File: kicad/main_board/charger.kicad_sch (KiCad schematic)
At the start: 72 parts, among them J4 BAT, J5 BAT_LINK, Q3 CSD17551Q3A, Q4 CSD17551Q3A, Q5 CSD17551Q3A, Q6 CSD17551Q3A, Q7 CSD25402Q3A, U4 BQ25703A

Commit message: add I2S link
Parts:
- added TP7: ~{BAT_INT}, TestPoint:TestPoint_Pad_D1.0mm, symbol Connector:TestPoint_Small
- renumbered TP9 to TP10, TP10 to TP11, TP11 to TP12, TP12 to TP13, TP7 to TP8, TP8 to TP9
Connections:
- net ~{BAT_INT}: no longer names the net of D2.2 (A), R22.1
- net ~{BAT_INT}: now also TP7.1
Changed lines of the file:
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@@
 	(title_block
 		(title "SW32 - Main Board")
-		(date "2024-05-22")
+		(date "2024-05-23")
 		(rev "1")
 		(company "saawsm")
@@
 	)
 	(junction
-		(at 59.69 186.69)
-		(diameter 0)
-		(color 0 0 0 0)
-	)
-	(junction
 		(at 143.51 55.88)
 		(diameter 0)
@@
 	)
 	(junction
+		(at 59.69 186.69)
+		(diameter 0)
+		(color 0 0 0 0)
+	)
+	(junction
 		(at 256.54 114.3)
 		(diameter 0)
@@
 	(wire
 		(pts
+			(xy 59.69 186.69) (xy 67.31 186.69)
+		)
+		(stroke
+			(width 0)
+			(type default)
+		)
+	)
+	(wire
+		(pts
 			(xy 106.68 134.62) (xy 115.57 134.62)
 		)
@@
 	(wire
 		(pts
-			(xy 59.69 186.69) (xy 67.31 186.69)
-		)
-		(stroke
-			(width 0)
-			(type default)
-		)
-	)
-	(wire
-		(pts
 			(xy 240.03 62.23) (xy 241.3 62.23)
 		)
@@
 		)
 	)
-	(hierarchical_label "~{BAT_INT}"
-		(shape output)
-		(at 67.31 186.69 0)
-		(fields_autoplaced yes)
-		(effects
-			(font
-				(size 1.27 1.27)
-			)
-			(justify left)
-		)
-	)
 	(hierarchical_label "SDA"
 		(shape bidirectional)
@@
 		(on_board yes)
 		(dnp no)
-		(property "Reference" "TP8"
+		(property "Reference" "TP9"
 			(at 113.03 136.906 0)
 			(effects
@@
 			(project "main_board"
 				(path "/8e1f1504-76c2-49e6-9261-3c1190503f8c/1076a657-0b13-48f5-b500-e72d30eb3a1f"
-					(reference "TP8")
+					(reference "TP9")
 					(unit 1)
 				)
@@
 		(dnp no)
 		(fields_autoplaced yes)
-		(property "Reference" "TP7"
+		(property "Reference" "TP8"
 			(at 104.14 125.7299 0)
 			(effects
@@
 			(project "main_board"
 				(path "/8e1f1504-76c2-49e6-9261-3c1190503f8c/1076a657-0b13-48f5-b500-e72d30eb3a1f"
-					(reference "TP7")
+					(reference "TP8")
 					(unit 1)
 				)
@@
 		(dnp no)
 		(fields_autoplaced yes)
-		(property "Reference" "TP11"
+		(property "Reference" "TP12"
 			(at 267.97 151.13 0)
 			(effects
@@
 			(project "main_board"
 				(path "/8e1f1504-76c2-49e6-9261-3c1190503f8c/1076a657-0b13-48f5-b500-e72d30eb3a1f"
-					(reference "TP11")
+					(reference "TP12")
 					(unit 1)
 				)
@@
 		(dnp no)
 		(fields_autoplaced yes)
-		(property "Reference" "TP9"
+		(property "Reference" "TP10"
 			(at 203.2 21.5899 0)
 			(effects
@@
 			(project "main_board"
 				(path "/8e1f1504-76c2-49e6-9261-3c1190503f8c/1076a657-0b13-48f5-b500-e72d30eb3a1f"
-					(reference "TP9")
+					(reference "TP10")
 					(unit 1)
 				)
@@
 		(dnp no)
 		(fields_autoplaced yes)
-		(property "Reference" "TP10"
+		(property "Reference" "TP11"
 			(at 217.17 116.84 90)
 			(effects
@@
 			(project "main_board"
 				(path "/8e1f1504-76c2-49e6-9261-3c1190503f8c/1076a657-0b13-48f5-b500-e72d30eb3a1f"
-					(reference "TP10")
+					(reference "TP11")
+					(unit 1)
+				)
+			)
+		)
+	)
+	(symbol
+		(lib_id "Connector:TestPoint_Small")
+		(at 67.31 186.69 0)
+		(mirror y)
+		(unit 1)
+		(exclude_from_sim no)
+		(in_bom no)
+		(on_board yes)
+		(dnp no)
+		(fields_autoplaced yes)
+		(property "Reference" "TP7"
+			(at 68.58 185.4199 0)
+			(effects
+				(font
+					(size 1.27 1.27)
+				)
+				(justify right)
+			)
+		)
+		(property "Value" "~{BAT_INT}"
+			(at 68.58 187.9599 0)
+			(effects
+				(font
+					(size 1.27 1.27)
+				)
+				(justify right)
+			)
+		)
+		(property "Footprint" "TestPoint:TestPoint_Pad_D1.0mm"
+			(at 62.23 186.69 0)
+			(effects
+				(font
+					(size 1.27 1.27)
+				)
+				(hide yes)
+			)
+		)
+		(property "Datasheet" "~"
+			(at 62.23 186.69 0)
+			(effects
+				(font
+					(size 1.27 1.27)
+				)
+				(hide yes)
+			)
+		)
+		(property "Description" "test point"
+			(at 67.31 186.69 0)
+			(effects
+				(font
+					(size 1.27 1.27)
+				)
+				(hide yes)
+			)
+		)
+		(property "MPN" ""
+			(at 67.31 186.69 0)
+			(effects
+				(font
+					(size 1.27 1.27)
+				)
+				(hide yes)
+			)
+		)
+		(property "MPN_ALT" ""
+			(at 67.31 186.69 0)
+			(effects
+				(font
+					(size 1.27 1.27)
+				)
+				(hide yes)
+			)
+		)
+		(property "LCSC" ""
+			(at 67.31 186.69 0)
+			(effects
+				(font
+					(size 1.27 1.27)
+				)
+				(hide yes)
+			)
+		)
+		(property "MOUSER" ""
+			(at 67.31 186.69 0)
+			(effects
+				(font
+					(size 1.27 1.27)
+				)
+				(hide yes)
+			)
+		)
+		(pin "1"
+		)
+		(instances
+			(project "main_board"
+				(path "/8e1f1504-76c2-49e6-9261-3c1190503f8c/1076a657-0b13-48f5-b500-e72d30eb3a1f"
+					(reference "TP7")
 					(unit 1)
 				)
@@
 		(dnp no)
 		(fields_autoplaced yes)
-		(property "Reference" "TP12"
+		(property "Reference" "TP13"
 			(at 275.59 151.13 0)
 			(effects
@@
 			(project "main_board"
 				(path "/8e1f1504-76c2-49e6-9261-3c1190503f8c/1076a657-0b13-48f5-b500-e72d30eb3a1f"
-					(reference "TP12")
+					(reference "TP13")
 					(unit 1)
 				)

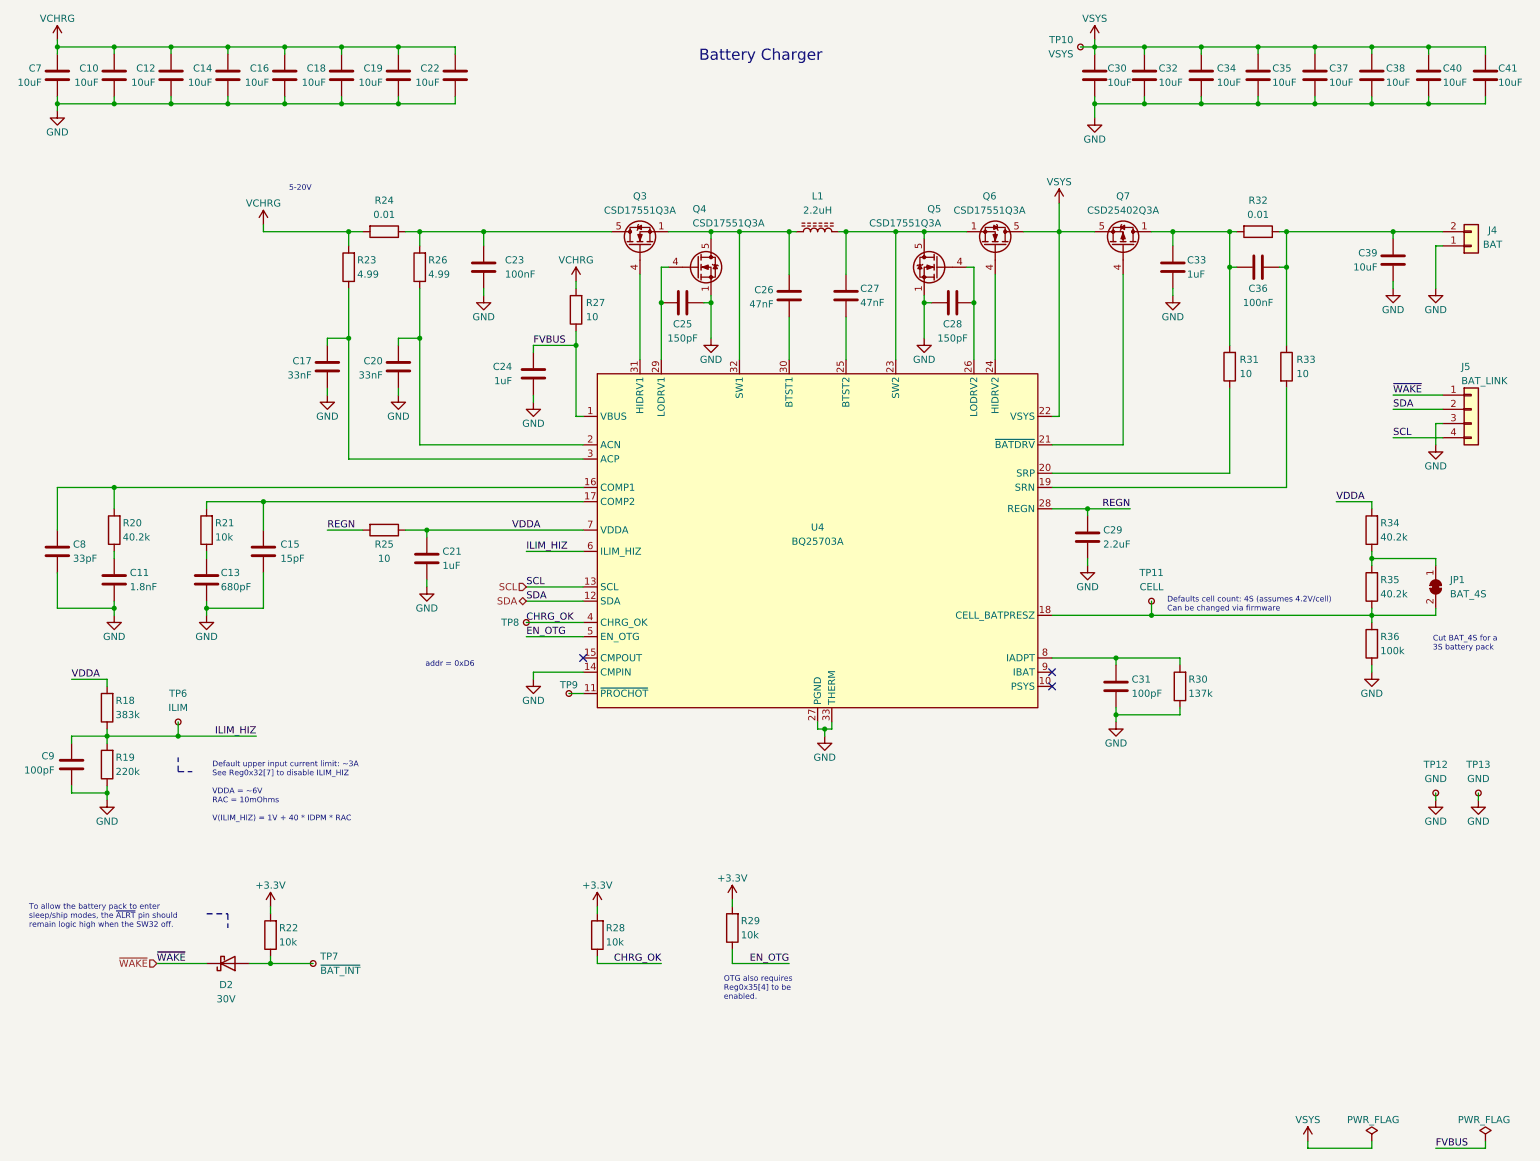
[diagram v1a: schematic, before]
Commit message: remove BAT_INT
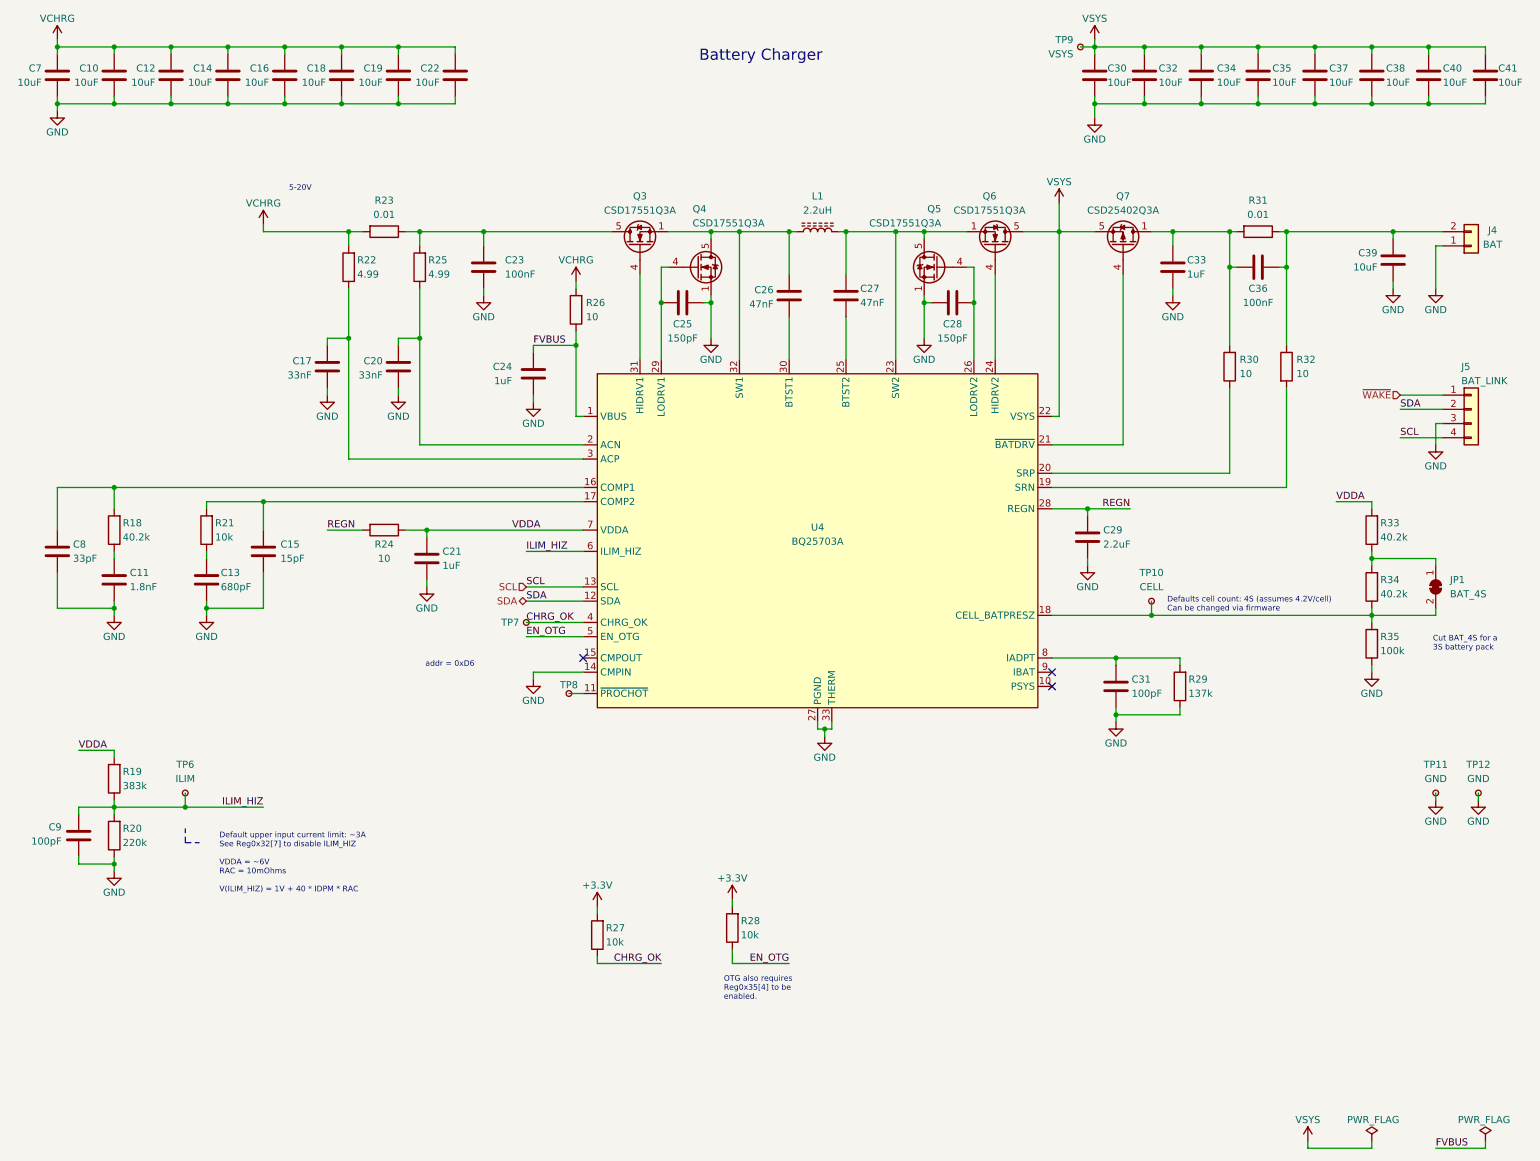
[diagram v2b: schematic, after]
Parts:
- removed D2: 30V, Diode_SMD:D_SOD-523, symbol Device:D_Schottky
- removed R22: 10k, Resistor_SMD:R_0603_1608Metric, symbol Device:R
- removed TP7: ~{BAT_INT}, TestPoint:TestPoint_Pad_D1.0mm, symbol Connector:TestPoint_Small
- renumbered R20 to R18, R18 to R19, R19 to R20, R23 to R22, R24 to R23, R25 to R24, R26 to R25, R27 to R26, R28 to R27, R29 to R28, R30 to R29, R31 to R30, R32 to R31, R33 to R32, R34 to R33, R35 to R34, R36 to R35, TP11 to TP10, TP12 to TP11, TP13 to TP12, TP8 to TP7, TP9 to TP8, TP10 to TP9
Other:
- note removed: "To allow the battery pack to enter sleep/ship modes, the ~{ALRT} pin should remain logic high when the SW32 off."
- moved on the sheet: C9, R19, R20, TP6

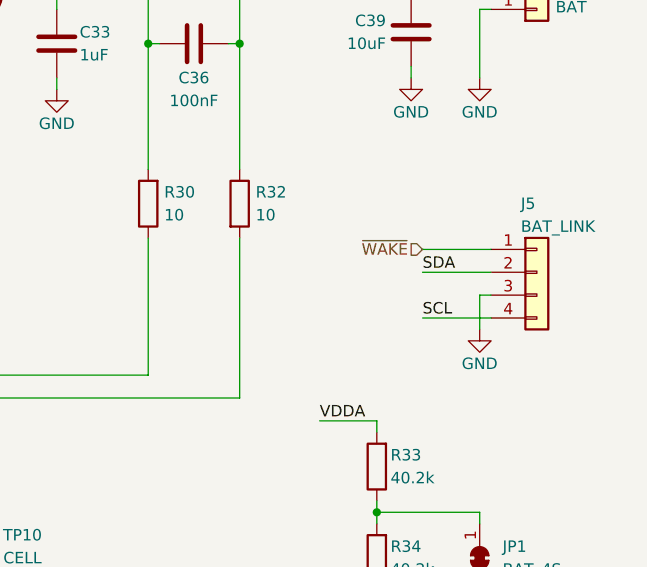
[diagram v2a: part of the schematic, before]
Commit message: fix BAT_LINK pinout for consistency
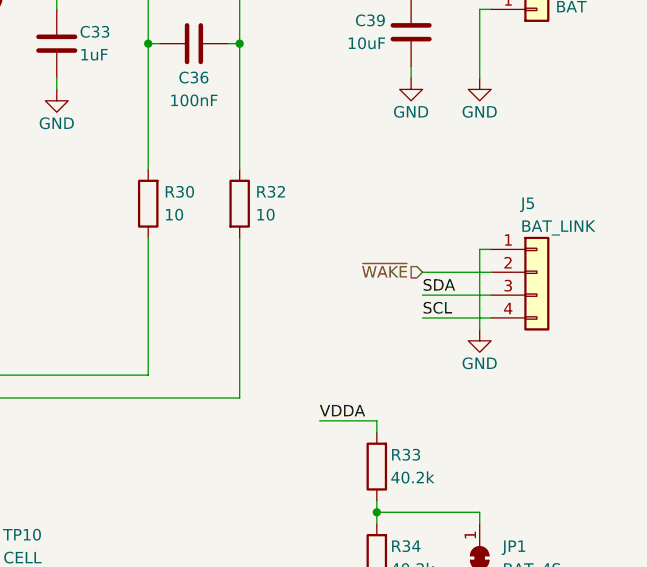
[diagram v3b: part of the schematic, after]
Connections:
- net GND: now also J5.1 (Pin_1); no longer J5.3 (Pin_3)
- net SDA: now also J5.3 (Pin_3); no longer J5.2 (Pin_2)
- net ~{WAKE}: now also J5.2 (Pin_2); no longer J5.1 (Pin_1)
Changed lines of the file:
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@@
 	(wire
 		(pts
-			(xy 267.97 90.17) (xy 269.24 90.17)
+			(xy 267.97 85.09) (xy 269.24 85.09)
 		)
 		(stroke
@@
 	(wire
 		(pts
-			(xy 267.97 93.98) (xy 267.97 90.17)
+			(xy 267.97 93.98) (xy 267.97 85.09)
 		)
 		(stroke
@@
 	(wire
 		(pts
-			(xy 261.62 85.09) (xy 269.24 85.09)
+			(xy 261.62 87.63) (xy 269.24 87.63)
 		)
 		(stroke
@@
 	(wire
 		(pts
-			(xy 261.62 87.63) (xy 269.24 87.63)
+			(xy 261.62 90.17) (xy 269.24 90.17)
 		)
 		(stroke
@@
 	)
 	(label "SDA"
-		(at 261.62 87.63 0)
+		(at 261.62 90.17 0)
 		(fields_autoplaced yes)
 		(effects
@@
 	(hierarchical_label "~{WAKE}"
 		(shape input)
-		(at 261.62 85.09 180)
+		(at 261.62 87.63 180)
 		(fields_autoplaced yes)
 		(effects

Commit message: update BOM prioritizing basic parts
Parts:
- added R84: 82k, Resistor_SMD:R_0603_1608Metric, symbol Device:R
- added R85: 1.2k, Resistor_SMD:R_0603_1608Metric, symbol Device:R
- added R86: 100k, Resistor_SMD:R_0603_1608Metric, symbol Device:R
- added R87: 10k, Resistor_SMD:R_0603_1608Metric, symbol Device:R
- C10, C12, C14, C16, C18, C19, C22, C30, C32, C34, C35, C37, C38, C39, C40, C41, C7: JLC (none) -> C440198; LCSC C2932476 -> (none); MOUSER 187-CL21A106KBYQNNE -> (none); MPN CL21A106KBYQNNE -> (none)
- C11: JLC (none) -> C318642; LCSC C318642 -> (none); MOUSER 187-CL10C182JB8NNNC -> (none); MPN CL10C182JB8NNNC -> (none)
- C13: JLC (none) -> C30816; LCSC C30816 -> (none); MOUSER 187-CL10C681JB8NNNC -> (none); MPN CL10C681JB8NNNC -> (none)
- C15: JLC (none) -> C1644; LCSC C1644 -> (none); MOUSER 187-CL10C150JB8NNNC -> (none); MPN CL10C150JB8NNNC -> (none)
- C17, C20: JLC (none) -> C21117; LCSC C21117 -> (none); MOUSER 187-CL10B333KB8NNNC -> (none); MPN CL10B333KB8NNNC -> (none)
- C21, C24, C33: JLC (none) -> C15849; LCSC C5199872 -> (none); MOUSER 187-CL10B105KB8NQNC -> (none); MPN CL10B105KB8NQNC -> (none)
- C23, C36: JLC (none) -> C14663; LCSC C1591 -> (none); MOUSER 187-CL10B104KB8NNNC -> (none); MPN CL10B104KB8NNNC -> (none)
- C25, C28: JLC (none) -> C37298; LCSC C37298 -> (none); MOUSER 187-CL10C151JB8NNNC -> (none); MPN CL10C151JB8NNNC -> (none)
- C26, C27: JLC (none) -> C1622; LCSC C1622 -> (none); MOUSER 187-CL10B473KB8NNNC -> (none); MPN CL10B473KB8NNNC -> (none)
- C29: JLC (none) -> C23630; LCSC C307463 -> (none); MOUSER 187-CL10A225KL8NNNC -> (none); MPN CL10A225KL8NNNC -> (none)
- C31, C9: JLC (none) -> C14858; LCSC C14858 -> (none); MOUSER 187-CL10C101JB8NNNC -> (none); MPN CL10C101JB8NNNC -> (none)
- C8: JLC (none) -> C1663; LCSC C1663 -> (none); MOUSER 187-CL10C330JB8NNNC -> (none); MPN CL10C330JB8NNNC -> (none)
- J4: footprint Connector_AMASS:AMASS_XT30UPB-F_1x02_P5.0mm_Vertical -> Connector_AMASS:AMASS_XT30UPB-M_1x02_P5.0mm_Vertical
- J5: footprint Connector_JST:JST_PH_B4B-PH-K_1x04_P2.00mm_Vertical -> Connector_JST:JST_XH_B4B-XH-A_1x04_P2.50mm_Vertical; LCSC (none) -> C7429634
- L1: JLC (none) -> C540967; LCSC C540967 -> (none); MOUSER 70-IHLP2525CZER2R2M1 -> (none); MPN IHLP2525CZER2R2M01 -> (none)
- Q3, Q4, Q5, Q6: JLC (none) -> C2876535; LCSC C2876535 -> (none); MOUSER 595-CSD17551Q3A -> (none); MPN CSD17551Q3A -> (none)
- Q7: JLC (none) -> C111356; LCSC C111356 -> (none); MOUSER 595-CSD25402Q3A -> (none); MPN CSD25402Q3A -> (none)
- R18, R33, R34: value 40.2k -> 39k; JLC (none) -> C23153; LCSC C137723 -> (none); MOUSER 603-RC0603FR-0740K2L -> (none); MPN RC0603FR-0740K2L -> (none)
- R19: value 383k -> 300k; JLC (none) -> C23024; LCSC C25816 -> (none); MOUSER 603-RC0603FR-07383KL -> (none); MPN RC0603FR-07383KL -> (none)
- R20: JLC (none) -> C22961; LCSC C22961 -> (none); MOUSER 603-RC0603FR-07220KL -> (none); MPN RC0603FR-07220KL -> (none)
- R21, R27, R28: JLC (none) -> C25804; LCSC C25804 -> (none); MOUSER 603-RC0603FR-0710KL -> (none); MPN RC0603FR-0710KL -> (none)
- R22, R25: JLC (none) -> C137704; LCSC C137704 -> (none); MOUSER 603-RC0603FR-074R99L -> (none); MPN RC0603FR-074R99L -> (none)
- R23, R31: JLC (none) -> C844910; LCSC C844910 -> (none); MOUSER 71-WSLP1206R0100FEA -> (none); MPN WSLP1206R0100FEA -> (none)
- R24, R26, R30, R32: JLC (none) -> C22859; LCSC C109318 -> (none); MOUSER 603-RC0603FR-0710RL -> (none); MPN RC0603FR-0710RL -> (none)
- R29: value 137k -> 27k; JLC (none) -> C22967; LCSC C22872 -> (none); MOUSER 603-RC0603FR-07137KL -> (none); MPN RC0603FR-07137KL -> (none)
- R35: JLC (none) -> C25803; LCSC C25803 -> (none); MOUSER 603-RC0603FR-07100KL -> (none); MPN RC0603FR-07100KL -> (none)
- U4: JLC (none) -> C188229; LCSC C188229 -> (none); MOUSER 595-BQ25703ARSNR -> (none); MPN BQ25703ARSNR -> (none)
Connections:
- net GND: now also R86.1; no longer R29.1
- net VDDA: now also R84.1; no longer R19.2
- net at C8.1, U4.16 (COMP1): now also R85.2; no longer R18.2
- new net: R18.2, R85.1
- new net: R19.2, R84.2
- new net: R86.2, R87.1
- new net: R29.1, R87.2
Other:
- note added: "137k changed to 100k+10k+27k to avoid basic part fee"
- note added: "383k changed to 300k+82k to avoid basic part fee Adjusted current limit ~2.98A"
- note added: "40.2k changed to 39k+1.2k to avoid basic part fee"
- moved on the sheet: C11, C8, R18

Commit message: add generation script
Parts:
- C10, C12, C14, C16, C18, C19, C22, C30, C32, C34, C35, C37, C38, C39, C40, C41, C7: JLC C440198 -> (none); LCSC (none) -> C440198; Service (none) -> PCBA
- C11: JLC C318642 -> (none); LCSC (none) -> C318642; Service (none) -> PCBA
- C13: JLC C30816 -> (none); LCSC (none) -> C30816; Service (none) -> PCBA
- C15: JLC C1644 -> (none); LCSC (none) -> C1644; Service (none) -> PCBA
- C17, C20: JLC C21117 -> (none); LCSC (none) -> C21117; Service (none) -> PCBA
- C21, C24, C33: JLC C15849 -> (none); LCSC (none) -> C15849; Service (none) -> PCBA
- C23, C36: JLC C14663 -> (none); LCSC (none) -> C14663; Service (none) -> PCBA
- C25, C28: JLC C37298 -> (none); LCSC (none) -> C37298; Service (none) -> PCBA
- C26, C27: JLC C1622 -> (none); LCSC (none) -> C1622; Service (none) -> PCBA
- C29: JLC C23630 -> (none); LCSC (none) -> C23630; Service (none) -> PCBA
- C31, C9: JLC C14858 -> (none); LCSC (none) -> C14858; Service (none) -> PCBA
- C8: JLC C1663 -> (none); LCSC (none) -> C1663; Service (none) -> PCBA
- J4, J5: Service (none) -> HandAssembly
- JP1, TP10, TP11, TP12, TP6, TP7, TP8, TP9: Service (none) -> PCBA;HandAssembly
- L1: JLC C540967 -> (none); LCSC (none) -> C540967; Service (none) -> PCBA
- Q3, Q4, Q5, Q6: JLC C2876535 -> (none); LCSC (none) -> C2876535; Service (none) -> PCBA
- Q7: JLC C111356 -> (none); LCSC (none) -> C111356; Service (none) -> PCBA
- R18, R33, R34: JLC C23153 -> (none); LCSC (none) -> C23153; Service (none) -> PCBA
- R19: JLC C23024 -> (none); LCSC (none) -> C23024; Service (none) -> PCBA
- R20: JLC C22961 -> (none); LCSC (none) -> C22961; Service (none) -> PCBA
- R21, R27, R28, R87: JLC C25804 -> (none); LCSC (none) -> C25804; Service (none) -> PCBA
- R22, R25: JLC C137704 -> (none); LCSC (none) -> C137704; Service (none) -> PCBA
- R23, R31: JLC C844910 -> (none); LCSC (none) -> C844910; Service (none) -> PCBA
- R24, R26, R30, R32: JLC C22859 -> (none); LCSC (none) -> C22859; Service (none) -> PCBA
- R29: JLC C22967 -> (none); LCSC (none) -> C22967; Service (none) -> PCBA
- R35, R86: JLC C25803 -> (none); LCSC (none) -> C25803; Service (none) -> PCBA
- R84: JLC C23254 -> (none); LCSC (none) -> C23254; Service (none) -> PCBA
- R85: JLC C22765 -> (none); LCSC (none) -> C22765; Service (none) -> PCBA
- U4: JLC C188229 -> (none); LCSC (none) -> C188229; Service (none) -> PCBA
